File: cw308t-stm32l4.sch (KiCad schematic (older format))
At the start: 17 parts, among them J1 CW308T_CONNBOARD, J2 Conn_02x03_Odd_Even, U1 STM32L432KCUx

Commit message: 2x5 pin header, minor improvements
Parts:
- J2: footprint Connector_PinHeader_2.54mm:PinHeader_2x03_P2.54mm_Vertical -> Connector_PinHeader_2.54mm:PinHeader_2x05_P2.54mm_Vertical; symbol Connector_Generic:Conn_02x03_Odd_Even -> Connector_Generic:Conn_02x05_Odd_Even
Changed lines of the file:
@@
 USB/CAN
 $Comp
-L Connector_Generic:Conn_02x03_Odd_Even J2
+L Connector_Generic:Conn_02x05_Odd_Even J2
 U 1 1 5D4646B0
-P 9450 5500
-F 0 "J2" H 9500 5817 50  0000 C CNN
-F 1 "Conn_02x03_Odd_Even" H 9500 5726 50  0000 C CNN
-F 2 "Connector_PinHeader_2.54mm:PinHeader_2x03_P2.54mm_Vertical" H 9450 5500 50  0001 C CNN
-F 3 "~" H 9450 5500 50  0001 C CNN
-	1    9450 5500
+P 9450 5600
+F 0 "J2" H 9500 5900 50  0000 C CNN
+F 1 "Conn_02x03_Odd_Even" H 9400 5300 50  0000 C CNN
+F 2 "Connector_PinHeader_2.54mm:PinHeader_2x05_P2.54mm_Vertical" H 9450 5600 50  0001 C CNN
+F 3 "~" H 9450 5600 50  0001 C CNN
+	1    9450 5600
 	1    0    0    -1
 $EndComp

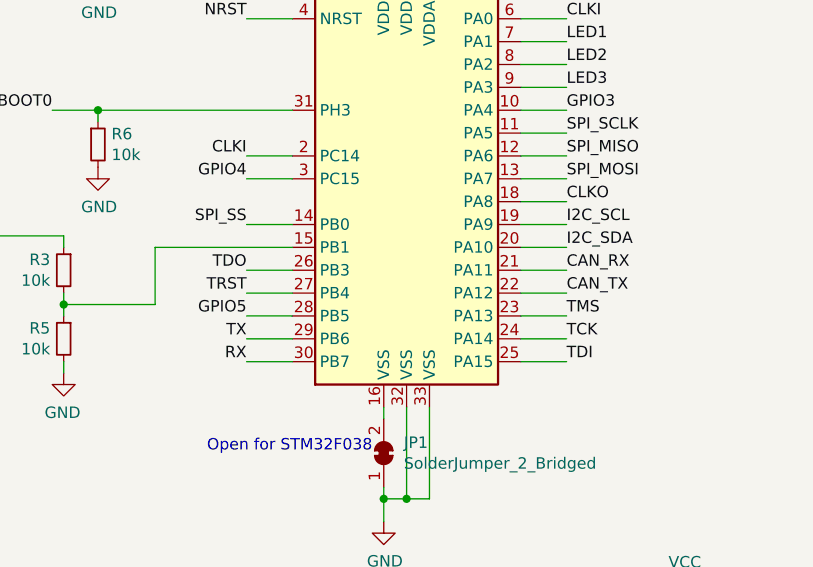
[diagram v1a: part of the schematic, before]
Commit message: Swap UART, I2C (see #1); add more visible pin 1 marker for STM32
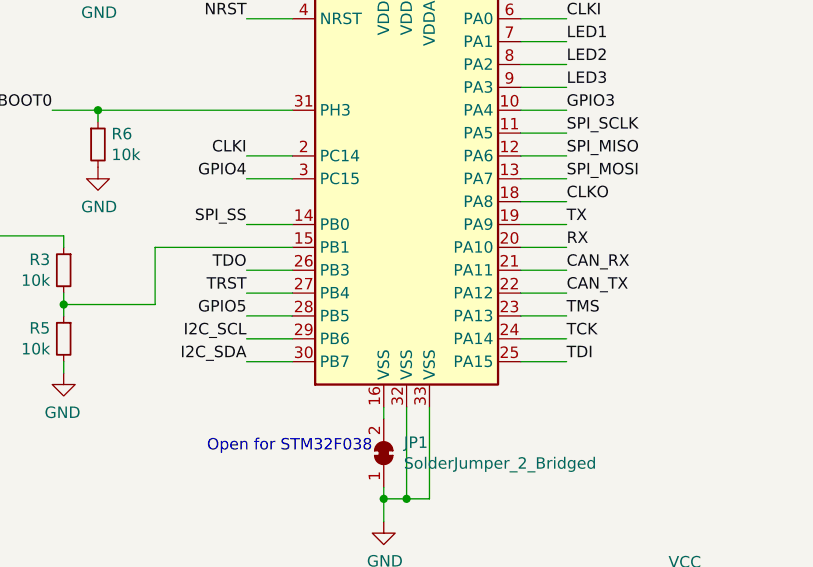
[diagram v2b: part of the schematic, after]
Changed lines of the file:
@@
 EESchema Schematic File Version 4
 LIBS:cw308t-stm32l4-cache
-EELAYER 29 0
+EELAYER 30 0
 EELAYER END
 $Descr A4 11693 8268
@@
 Wire Wire Line
 	2050 2400 1950 2400
-Text Label 8200 3500 2    50   ~ 0
+Text Label 9600 3000 0    50   ~ 0
 TX
 Wire Wire Line
 	8200 3600 8400 3600
-Text Label 8200 3600 2    50   ~ 0
+Text Label 9600 3100 0    50   ~ 0
 RX
 Wire Wire Line
@@
 	5850 2800 5850 2700
 Connection ~ 5850 2700
-Text Label 9600 3000 0    50   ~ 0
+Text Label 8200 3500 2    50   ~ 0
 I2C_SCL
-Text Label 9600 3100 0    50   ~ 0
+Text Label 8200 3600 2    50   ~ 0
 I2C_SDA
 Wire Wire Line

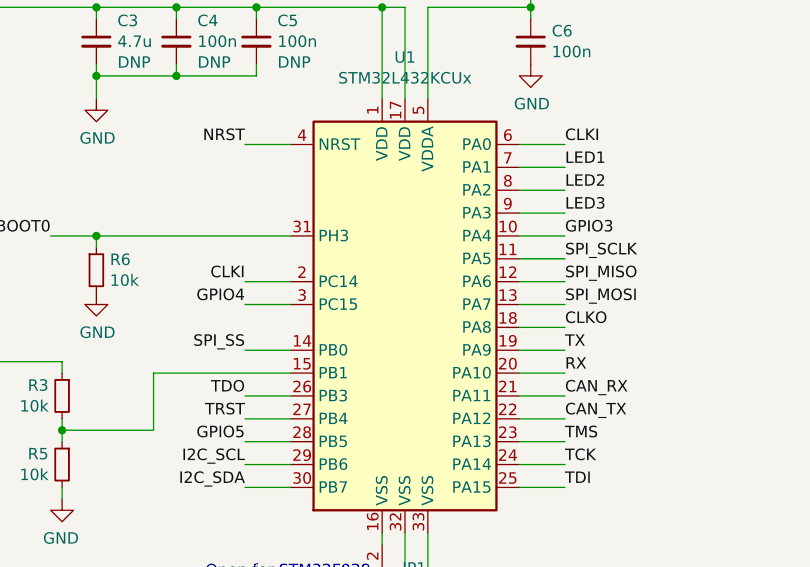
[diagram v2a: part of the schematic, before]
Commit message: Swap GPIO3 and SPI_SS (see #1)
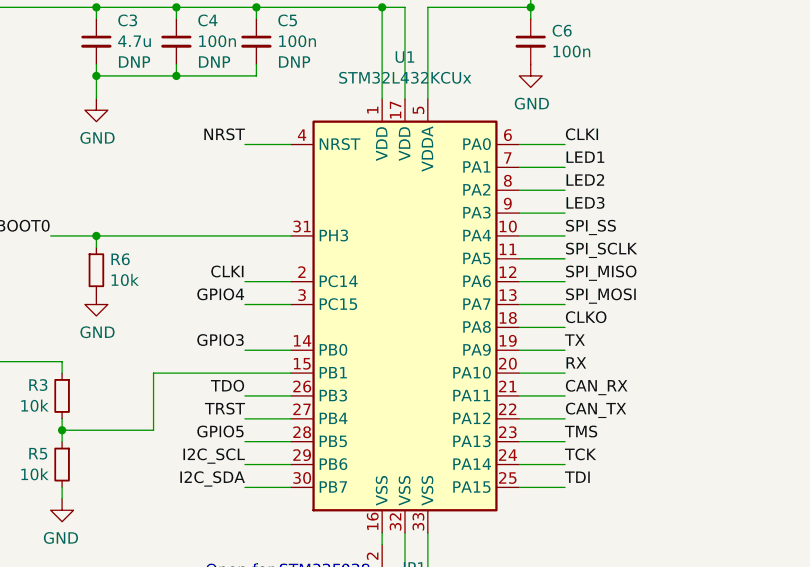
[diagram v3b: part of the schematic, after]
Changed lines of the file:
@@
 Wire Wire Line
 	8400 3500 8200 3500
-Text Label 9600 2500 0    50   ~ 0
+Text Label 8200 3000 2    50   ~ 0
 GPIO3
 Text Label 8200 2800 2    50   ~ 0
@@
 Wire Wire Line
 	7800 3100 8400 3100
-Text Label 8200 3000 2    50   ~ 0
+Text Label 9600 2500 0    50   ~ 0
 SPI_SS
 Wire Wire Line
